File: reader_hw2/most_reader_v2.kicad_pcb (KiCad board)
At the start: 2 copper layers, 95 x 26.5 mm, 56 parts, among them J1 1-1394640-1, J4 VBAT_IN, J6 PLT237/T10WH, M1 Tang Nano 20K, U1 74LVC1G34, U3 74LVC1G125, U4 74LVC1G123, U5 TPS7B8133DRV, U6 LMR38020F

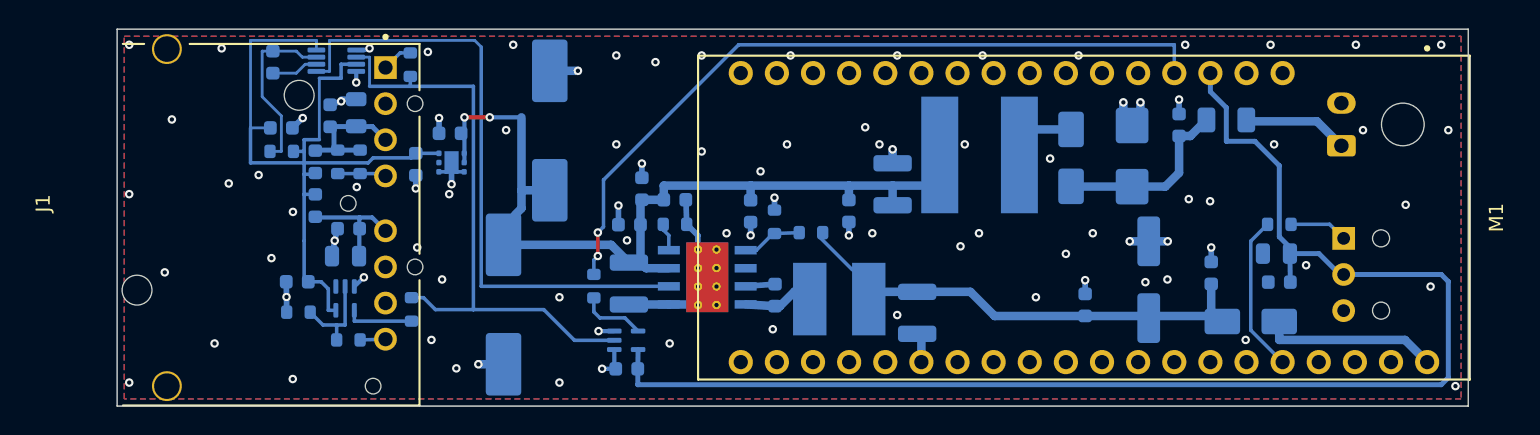
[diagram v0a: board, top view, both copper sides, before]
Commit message: reader v2.0: modernized - the board 84.9 mm, C45 8x10, the module on nine pins
The user re-placed the parts in KiCad round by round and the copper followed:
- power section: C6 between U6 and L1 (SW node 3.7 mm), C4 straight onto
  U6's VIN and exposed pad; C45 moved to the VBAT_P bus by U6
- C45 47u 63V in 8x10 (SamYoung MVK, C165628) instead of 100u 10x10.5, made
  in gen_reader2.py; check_v2_circuit allows exactly this change
- the module four header pins nearer J1, the board and tube 84.9 mm, J4 and
  J6 with the far edge; its footprint cut to nine pads (TANG_PINS)
- far end placed by the user: D3 lying with SPDIF between its pads, 3V3_SW
  from pin 7 between F1's and R28's pads; /WAKE and RX_BUF as diagonals
- 496 mm of copper (541), 75 vias (96), the same two top-layer hops

fab, caps, the kit READMEs and the READMEs regenerated for 84.9 mm.

Co-Authored-By: Claude Opus 5.5 <noreply@anthropic.com>
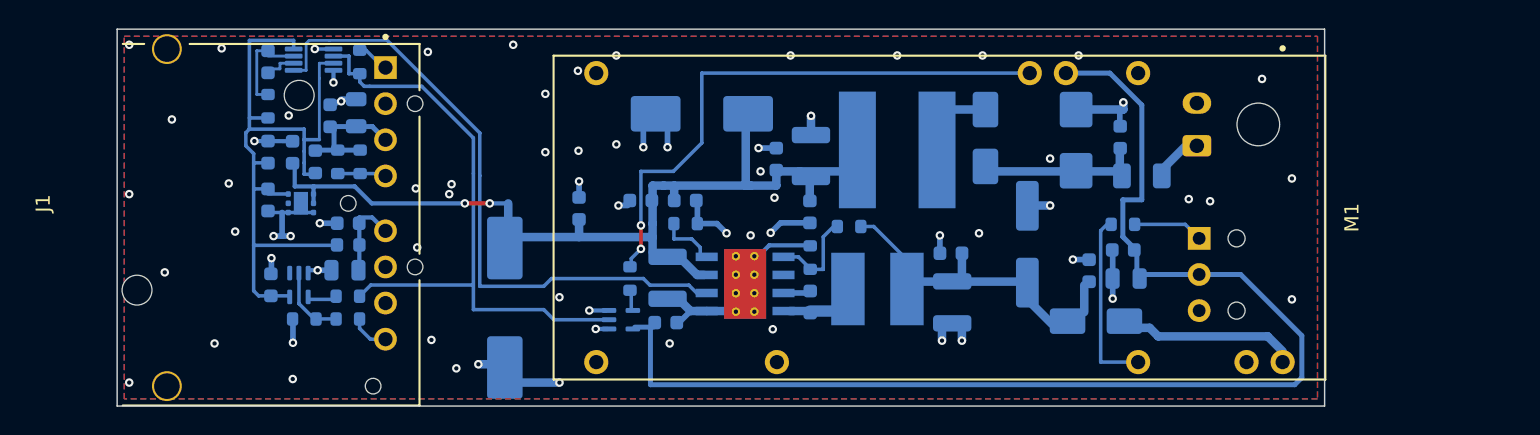
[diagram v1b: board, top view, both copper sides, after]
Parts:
- C45: value 100u 63V -> 47u 63V; footprint Capacitor_SMD:CP_Elec_10x10.5 -> Capacitor_SMD:CP_Elec_8x10
- moved C31 11.2 mm to (133.3, 109.0)
- moved C46 11.2 mm to (74.9, 102.1), turned to 90 degrees
- moved R28 11.0 mm to (133.2, 107.2)
- moved U5 11.0 mm to (75.4, 105.7)
- moved D3 10.9 mm to (131.3, 114.0)
- moved C45 10.8 mm to (103.6, 99.4), turned to 180 degrees
- moved C32 10.7 mm to (133.5, 111.0)
- moved C3 10.7 mm to (73.1, 105.5)
- moved M1 10.2 mm to (120.3, 106.7)
- moved J4 10.2 mm to (138.4, 101.7)
- moved J6 10.2 mm to (138.6, 110.7)
- moved C64 10.1 mm to (121.1, 109.2), turned to 180 degrees
- moved C63 8.89 mm to (126.5, 108.6)
- moved C85 8.59 mm to (130.9, 110.4)
- moved F1 7.13 mm to (134.6, 103.8)
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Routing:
- net GND: track 44.9 -> 59.2 mm, vias 92 -> 71
- net 5V_SW: track 29.8 -> 16.2 mm
- net /RX_IN: track 53.0 -> 39.9 mm
- net 3V3_SW: track 96.6 -> 86.6 mm
- net Net-(U4-REXT/CEXT): track 12.4 -> 6.45 mm
- net Net-(J4-VBAT): track 7.40 -> 2.47 mm
- net 3V3_AON: track 53.8 -> 49.9 mm
- net Net-(U3-Y): track 4.66 -> 1.25 mm
- net Net-(U1-Y): track 4.78 -> 1.96 mm
- net Net-(J1-RXVCC): track 8.04 -> 5.94 mm
- net Net-(D1-A): track 13.0 -> 11.1 mm
- net Net-(U1-A): track 6.59 -> 4.96 mm
- net Net-(U6-RT/SYNC): track 1.98 -> 3.60 mm
- net Net-(U6-FB): track 4.25 -> 5.69 mm
- net VBAT_P: track 56.9 -> 58.3 mm
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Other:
- board size 95 x 26.5 mm -> 84.9 x 26.5 mm
